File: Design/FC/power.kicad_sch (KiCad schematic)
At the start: 70 parts, among them J1 XT60PW-M, U1 STM32H747BIT6, U2 INA219AIDCNT

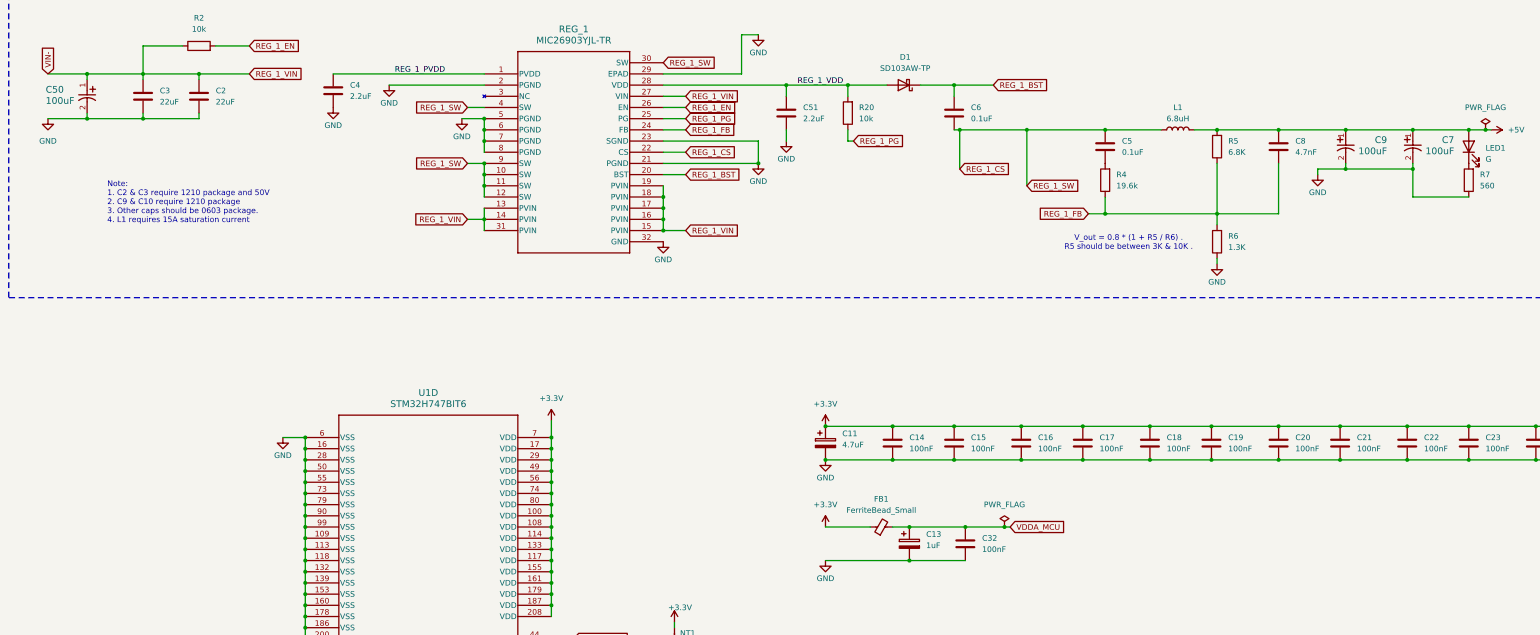
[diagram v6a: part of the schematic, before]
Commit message: finished filling out bom
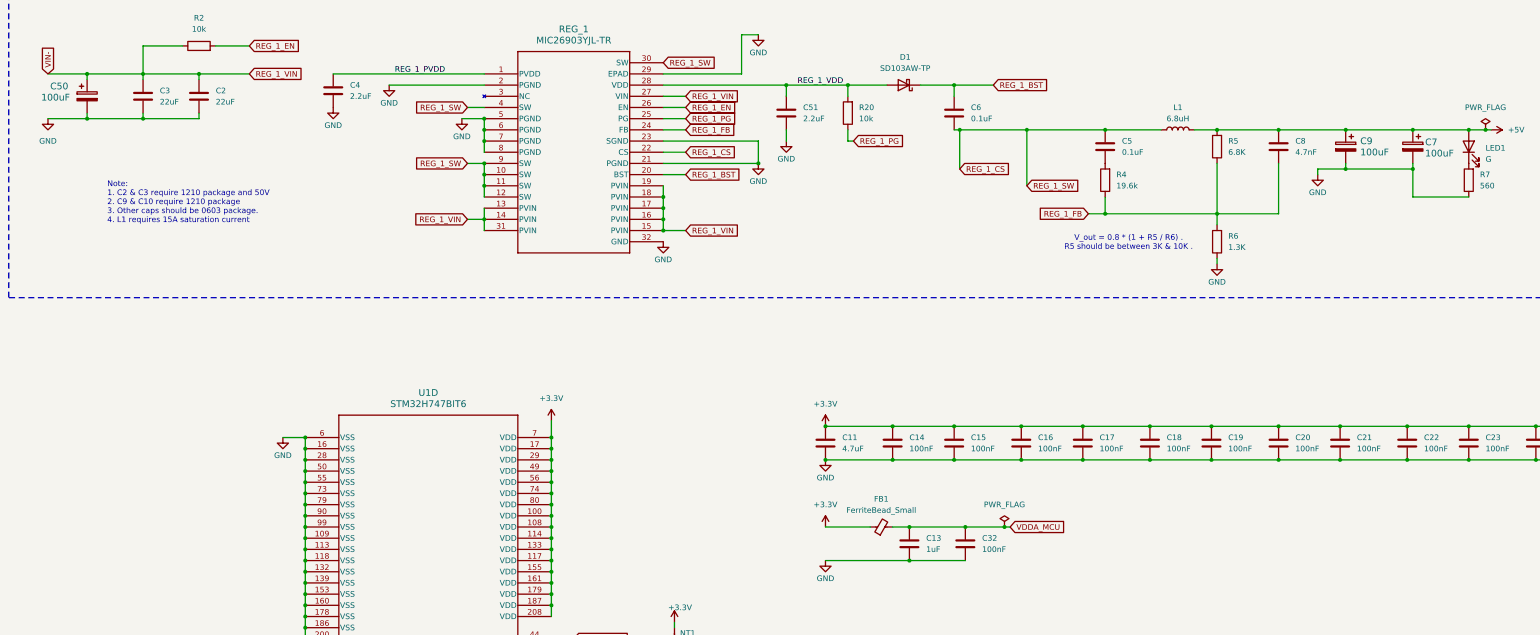
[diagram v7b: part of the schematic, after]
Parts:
- C11: symbol Device:C_Polarized -> Device:C
- C13: symbol Device:C_Polarized -> Device:C; Manufacturer_Name KYOCERA AVX -> Murata Electronics; Manufacturer_Part_Number TACL105K016RTA -> GRM188R61A105KA61D
- C50, C7, C9: symbol CAP_6.3 X 7.7_PAN:EEE-FPV101XAP -> Device:C_Polarized
- LED1, LED8: Manufacturer_Name Dialight -> Lite-On Inc.; Manufacturer_Part_Number 5990081007F -> LTW-C190DA5
- R1: Manufacturer_Name (none) -> YAGEO; Manufacturer_Part_Number (none) -> PE2512FKE7W0R01Z; PACKAGE_TYPE (none) -> SMD 2512
- R2, R20: Manufacturer_Name (none) -> Panasonic Electronic Components; Manufacturer_Part_Number (none) -> ERJ-T06J103V; PACKAGE_TYPE (none) -> SMD 0805
- R3: Manufacturer_Name (none) -> Panasonic Electronic Components; Manufacturer_Part_Number (none) -> ERJ-PA3F5600V; PACKAGE_TYPE (none) -> SMD 0603
- R4: Manufacturer_Name (none) -> Panasonic Electronic Components; Manufacturer_Part_Number (none) -> ERA-3AEB1962V; PACKAGE_TYPE (none) -> SMD 0603
- R5: Manufacturer_Name (none) -> Panasonic Electronic Components; Manufacturer_Part_Number (none) -> ERA-6ARB682V; PACKAGE_TYPE (none) -> SMD 0805
- R6: Manufacturer_Name (none) -> Stackpole Electronics Inc; Manufacturer_Part_Number (none) -> RMCF0805FT1K30; PACKAGE_TYPE (none) -> SMD 0805
- R7: Manufacturer_Name (none) -> TE Connectivity Passive Product; Manufacturer_Part_Number (none) -> CRGP0603F560R; PACKAGE_TYPE (none) -> SMD 0603
- REG_1: Manufacturer_Name (none) -> Microchip Technology; Manufacturer_Part_Number (none) -> MIC26903YJL-TR; PACKAGE_TYPE (none) -> 28QFN
- REG_2: Manufacturer_Name (none) -> STMicroelectronics; Manufacturer_Part_Number (none) -> LD39200PU33R; PACKAGE_TYPE (none) -> 6-DFN
- U1: Manufacturer_Name (none) -> STMicroelectronics; Manufacturer_Part_Number (none) -> STM32H747BIT6; PACKAGE_TYPE (none) -> 208LQFP
- U2: Manufacturer_Name (none) -> Texas Instruments; Manufacturer_Part_Number (none) -> INA219AIDCNT; PACKAGE_TYPE (none) -> SOT23-8
